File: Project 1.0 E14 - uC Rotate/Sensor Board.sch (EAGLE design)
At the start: 98 parts, among them IC1 LT1963EST-1.5, IC2 LT1963EST-1.5, IC4 LT1963EST-1.5

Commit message: Sensor Test Board: Selected humididty sensor and connected all relevent traces, added two humidity sensors to the libray (Si7005, Si7013). Changed hibernation module crystal to a 2-SMD package and rearanged relevent areas. Added 3 indicator LEDs to pins 57 - 59. Renamed and cleaned up schematic pages (now 7 pages labled by sensor type as apposed to manufacturer. Removed all 3.0V traces and supply and repplaced by 3.3V supply. Most 3.3V traces now routed but waiting for final power consuption calculations before completion. Changed power and programing connectors to smaller profile connectors (1 mm pitch) reducing required space, and cleaned up respective areas. Moved MAG3110 to top of board to for greater seperation from Si7013.
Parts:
- removed U$16: 5023520200, Kas-Connectors:5023520200
- removed U$20: 5023520410, Kas-Connectors:5023520410
- added J1: 501568-0207, Kas-Connectors:501568-0207
- added LED2, LED3, LED4: Green, eagle-ltspice:LED_ESML0603
- added R12, R13, R14: 10k, Kas-Passives:RESISTOR
- added U$7: 501568-0407, Kas-Connectors:501568-0407
- U$12: device Kas-Crystal:AB26TRB -> Kas-Crystal:ABS07L
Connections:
- removed net N$13: C41.2, C42.1, U$11.GNDX
- new net IND-LED-1: LED2.A, U$11.PE4
- new net IND-LED-2: LED3.A, U$11.PB4
- new net IND-LED-3: LED4.A, U$11.PB5
- new net N$29: LED4.C, R14.2
- new net N$31: LED3.C, R13.2
- new net N$35: LED2.C, R12.2
- net 3.0V: no longer R9.2, U$17.VDD_IO, U$2.VDDIO
- net 3.3V: now also U$17.VDD_IO, U$2.VDDIO
- net GND: now also C41.2, C42.1, J1.1, R12.1, R13.1, R14.1, R9.2, U$11.GNDX; no longer U$16.1
- net N$19: now also J1.2; no longer U$16.2
- net SWCLK: now also U$7.1; no longer U$20.1
- net SWDIO: now also U$7.2; no longer U$20.2
- net SWO: now also U$7.4; no longer U$20.4
- net TDI: now also U$7.3; no longer U$20.3
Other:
- moved on the sheet: LED1, R7

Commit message: Sensor Test Board: All parts have had their connections reviewed and tickets have been creted were necesery. Componnet footprints that needed checking have been checked and corrected as needed. Any misnamed pads have also been corrected. Missing net names were named and updated.
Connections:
- net CS-ADT7301 renamed !CS-ADT7301
- net CS-ADXL362 renamed !CS-ADXL362
- removed net 3.0V: IC1G$1.OUT
- removed net CS-H3LIS331DLTR: U$2.CS, U$21.1
- removed net CS-LIS3DH: U$21.6, U$9.CS
- removed net CS-LPS331: U$21.8, U$4.CS
- removed net CS-LS3GD20: U$21.7, U$3.CS
- removed net CS-LSM303: U$21.5, U$6.CS
- removed net CS-LSM9D30-G: U$17.CS_G, U$21.2
- removed net CS-LSM9DS0-XM: U$17.CS_XM, U$21.3
- removed net CS-MAX21000: U$19.CS, U$21.4
- removed net N$2: C52.1, U$15.VDD
- new net !CS-H3LIS331DLTR: U$2.!CS, U$21.1
- new net !CS-LIS3DH: U$21.6, U$9.!CS
- new net !CS-LPS331: U$21.8, U$4.!CS
- new net !CS-LS3GD20: U$21.7, U$3.!CS
- new net !CS-LSM303: U$21.5, U$6.!CS
- new net !CS-LSM9D30-G: U$17.!CS_G, U$21.2
- new net !CS-LSM9DS0-XM: U$17.!CS_XM, U$21.3
- new net !CS-MAX21000: U$19.!CS, U$21.4
- net 3.3V: now also C52.1, U$15.VDD, U$19.VDDIO, U$2.RSVD#1, U$22.VSNS
- net GND: now also U$10.RSVD$1, U$19.RSVD#0, U$2.RSVD#0, U$8.NC
- net SD-CS: now also U$18.!CS; no longer U$18.CS
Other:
- moved on the sheet: C52, U$21

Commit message: Sensor Test Board: Closed tickets 2, 17, 18, 21, 25 and 26. Changed sensor's designations to U from undifined.
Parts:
- renumbered U$1 to U1, U$10 to U10, U$11 to U11, U$14 to U14, U$15 to U15, U$17 to U17, U$18 to J3, U$19 to U19, U$2 to U2, U$21 to U21, U$22 to U22, U$3 to U3, U$4 to U4, U$5 to U5, U$6 to U6, U$7 to U7, U$8 to U8, U$9 to U9
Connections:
- removed net DEN-L3GD: U3.DEN
- net GND: now also U11.!WAKE, U11.PD4, U11.PD5, U3.DEN

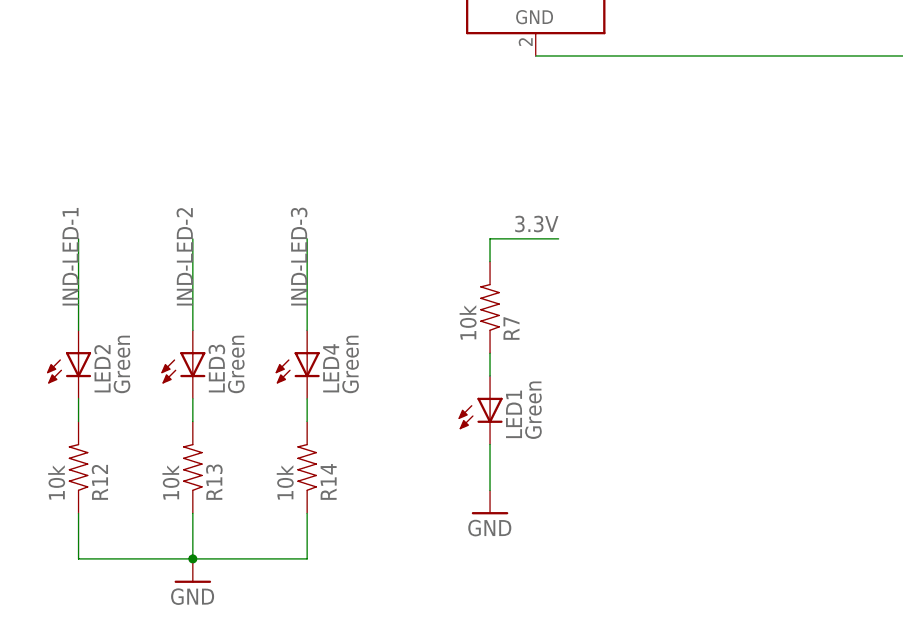
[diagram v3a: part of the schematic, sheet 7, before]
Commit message: Sensor Test Board: Resolved tickets 23, 20 and 19. The UART connection was moved to PIN 43 and 44 from 45,46 and a connector was added while the test points were moved lower to accomidate the connector.The indicator LEDs were moved from PB4, PB5 and PE4 to PB0 - PB3 with the addition one one more indication LED. The STLM20 was also moved to resolve ticket 19 and is now placed closer to PB4.
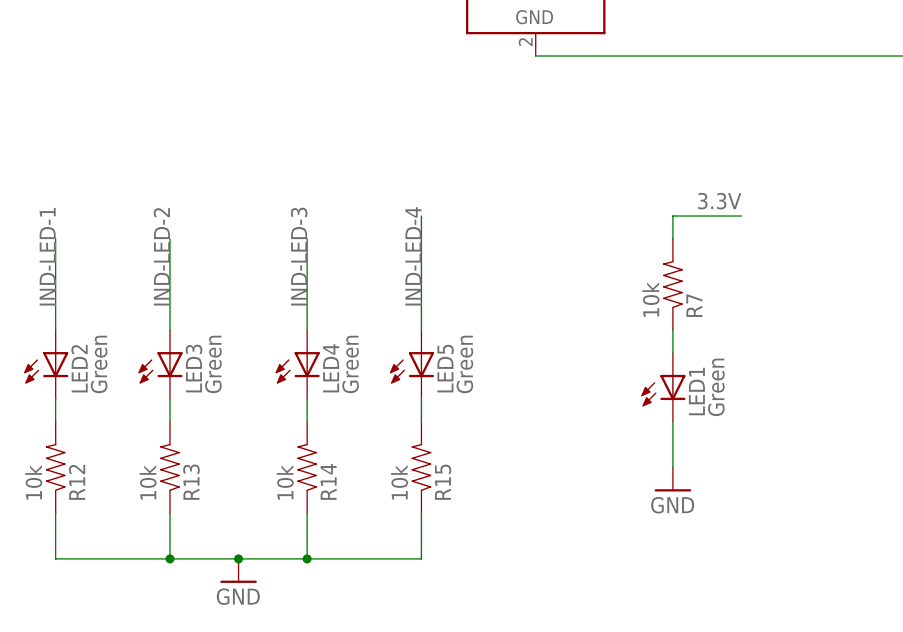
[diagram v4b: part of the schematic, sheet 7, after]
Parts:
- added J2: 501568-0207, Kas-Connectors:501568-0207
- added LED5: Green, eagle-ltspice:LED_ESML0603
- added R15: 10k, Kas-Passives:RESISTOR
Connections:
- removed net U1RX: TP8.P$1, U11.PB0
- removed net U1TX: TP7.P$1, U11.PB1
- new net IND-LED-4: LED5.A, U11.PB3
- new net N$18: LED5.C, R15.2
- new net U6RX: J2.1, TP8.P$1, U11.PD4
- new net U6TX: J2.2, TP7.P$1, U11.PD5
- net ANALOG-OUT-STLM20: now also U11.PB4; no longer U11.PB3
- net GND: now also R15.1, U17.INT_G; no longer R9.2, U11.PD4, U11.PD5
- net IND-LED-1: now also U11.PB0; no longer U11.PE4
- net IND-LED-2: now also U11.PB1; no longer U11.PB4
- net IND-LED-3: now also U11.PB2; no longer U11.PB5
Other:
- moved on the sheet: LED1, LED2, LED3, R11, R12, R13, R7, R9, TP7, TP8

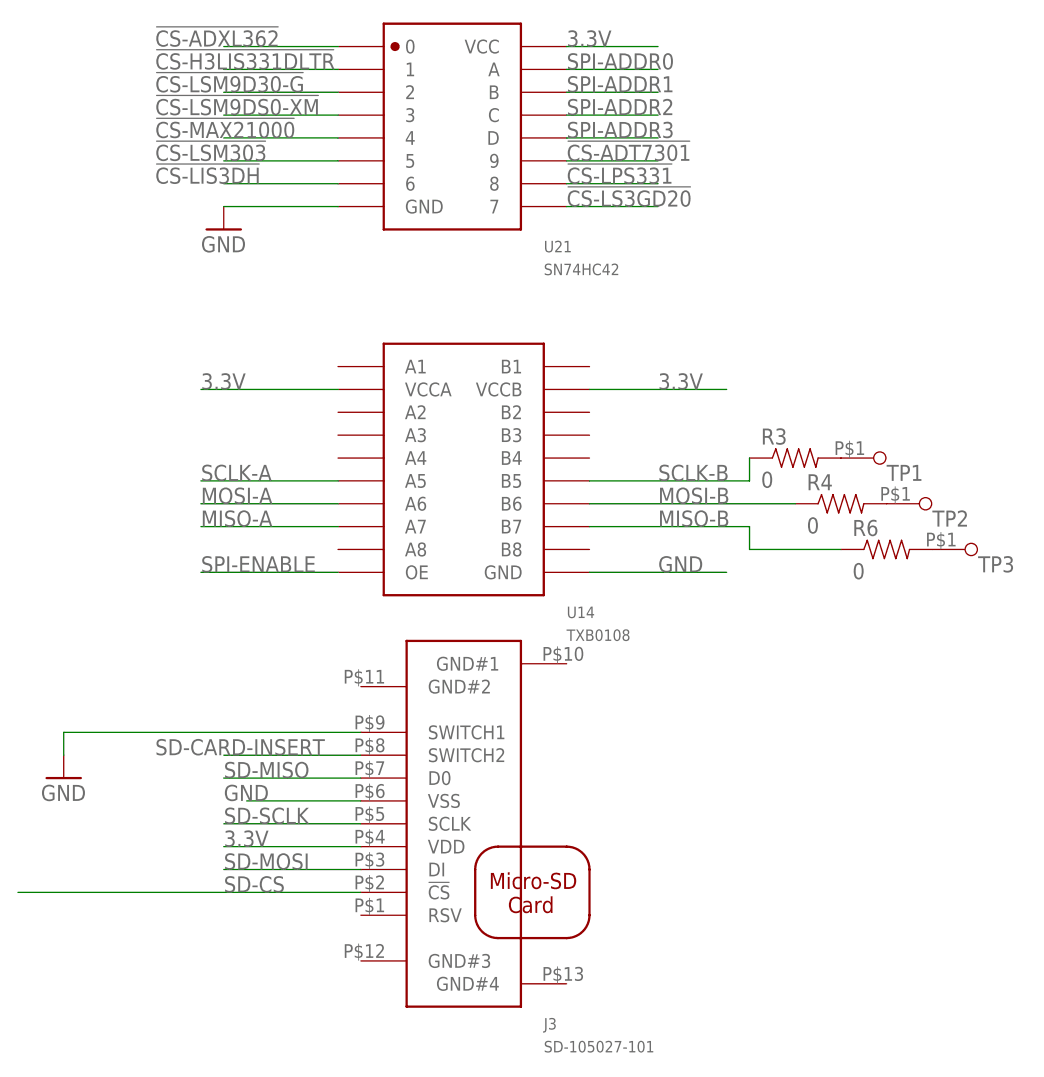
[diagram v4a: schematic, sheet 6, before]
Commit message: Sensor Test Board: Moved connections on TXB0108 to allow for simpler grounding of unused connections
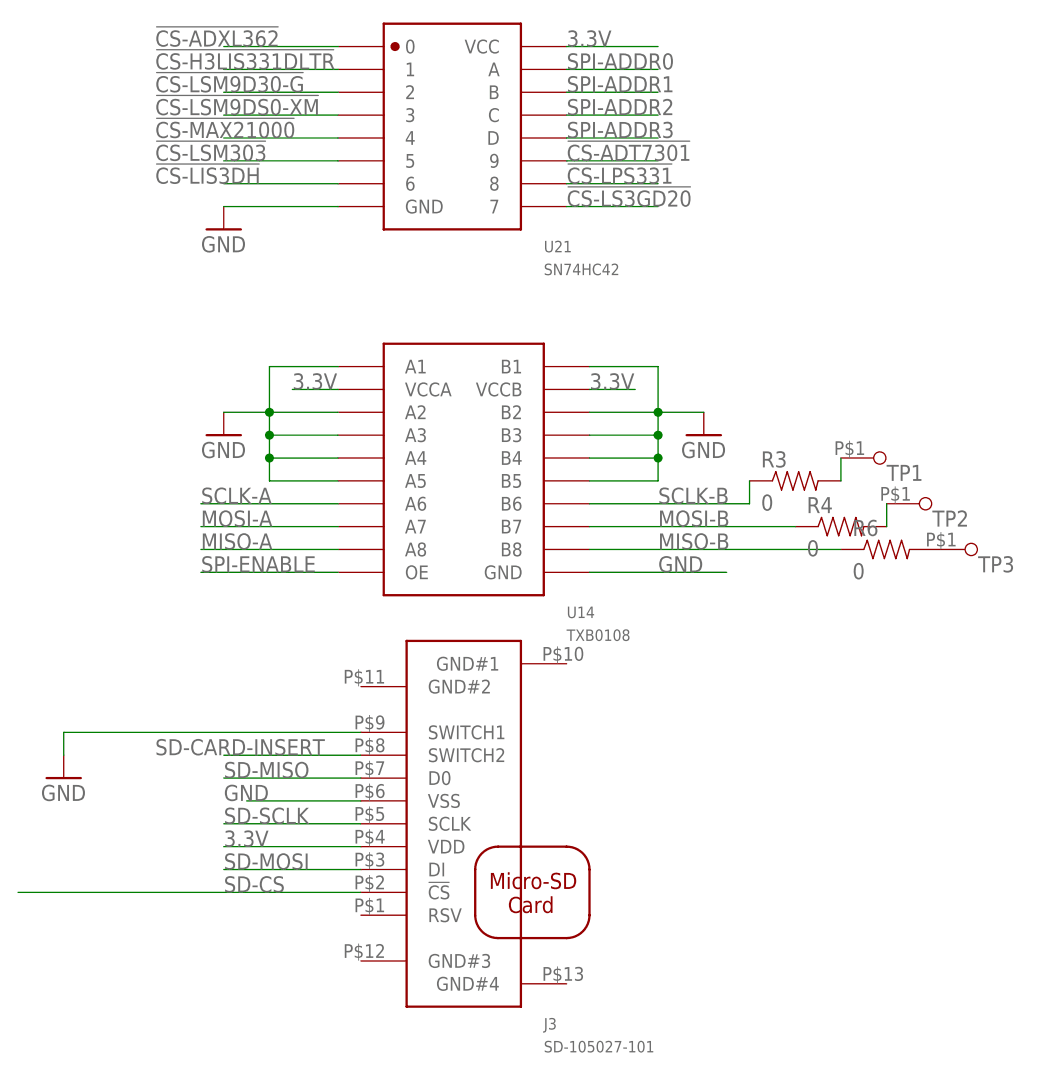
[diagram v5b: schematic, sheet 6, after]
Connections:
- net GND: now also U14.A1, U14.A2, U14.A3, U14.A4, U14.A5, U14.B1, U14.B2, U14.B3, U14.B4, U14.B5
- net MISO-A: now also U14.A8; no longer U14.A7
- net MISO-B: now also U14.B8; no longer U14.B7
- net MOSI-A: now also U14.A7; no longer U14.A6
- net MOSI-B: now also U14.B7; no longer U14.B6
- net SCLK-A: now also U14.A6; no longer U14.A5
- net SCLK-B: now also U14.B6; no longer U14.B5
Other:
- moved on the sheet: R3, R4
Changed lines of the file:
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@@
 <part name="LED5" library="eagle-ltspice" deviceset="LED_E" device="SML0603" value="Green"/>
 <part name="R15" library="Kas-Passives" deviceset="RESISTOR" device="" value="10k"/>
+<part name="GND50" library="SparkFun-Aesthetics" deviceset="GND" device=""/>
+<part name="GND51" library="SparkFun-Aesthetics" deviceset="GND" device=""/>
 </parts>
 <sheets>
@@
 <instance part="TP2" gate="G$1" x="53.34" y="-5.08"/>
 <instance part="TP3" gate="G$1" x="58.42" y="-10.16"/>
-<instance part="R3" gate="G$1" x="38.1" y="0"/>
-<instance part="R4" gate="G$1" x="43.18" y="-5.08"/>
+<instance part="R3" gate="G$1" x="38.1" y="-2.54"/>
+<instance part="R4" gate="G$1" x="43.18" y="-7.62"/>
 <instance part="R6" gate="G$1" x="48.26" y="-10.16"/>
 <instance part="U21" gate="G$1" x="0" y="35.56"/>
 <instance part="GND11" gate="1" x="-25.4" y="25.4"/>
+<instance part="GND50" gate="1" x="-25.4" y="2.54"/>
+<instance part="GND51" gate="1" x="27.94" y="2.54"/>
 </instances>
 <busses>
@@
 <pinref part="GND11" gate="1" pin="GND"/>
 </segment>
+<segment>
+<pinref part="U14" gate="G$1" pin="A2"/>
+<wire x1="-12.7" y1="5.08" x2="-20.32" y2="5.08" width="0.1524" layer="91"/>
+<pinref part="U14" gate="G$1" pin="A3"/>
+<wire x1="-20.32" y1="5.08" x2="-20.32" y2="2.54" width="0.1524" layer="91"/>
+<wire x1="-20.32" y1="2.54" x2="-12.7" y2="2.54" width="0.1524" layer="91"/>
+<pinref part="U14" gate="G$1" pin="A4"/>
+<wire x1="-12.7" y1="0" x2="-20.32" y2="0" width="0.1524" layer="91"/>
+<wire x1="-20.32" y1="0" x2="-20.32" y2="2.54" width="0.1524" layer="91"/>
+<junction x="-20.32" y="2.54"/>
+<pinref part="U14" gate="G$1" pin="A5"/>
+<wire x1="-12.7" y1="-2.54" x2="-20.32" y2="-2.54" width="0.1524" layer="91"/>
+<wire x1="-20.32" y1="-2.54" x2="-20.32" y2="0" width="0.1524" layer="91"/>
+<junction x="-20.32" y="0"/>
+<wire x1="-20.32" y1="5.08" x2="-20.32" y2="10.16" width="0.1524" layer="91"/>
+<junction x="-20.32" y="5.08"/>
+<pinref part="U14" gate="G$1" pin="A1"/>
+<wire x1="-20.32" y1="10.16" x2="-12.7" y2="10.16" width="0.1524" layer="91"/>
+<pinref part="GND50" gate="1" pin="GND"/>
+<wire x1="-20.32" y1="5.08" x2="-25.4" y2="5.08" width="0.1524" layer="91"/>
+</segment>
+<segment>
+<pinref part="U14" gate="G$1" pin="B2"/>
+<wire x1="15.24" y1="5.08" x2="22.86" y2="5.08" width="0.1524" layer="91"/>
+<wire x1="22.86" y1="5.08" x2="22.86" y2="2.54" width="0.1524" layer="91"/>
+<pinref part="U14" gate="G$1" pin="B3"/>
+<wire x1="22.86" y1="2.54" x2="15.24" y2="2.54" width="0.1524" layer="91"/>
+<pinref part="U14" gate="G$1" pin="B4"/>
+<wire x1="15.24" y1="0" x2="22.86" y2="0" width="0.1524" layer="91"/>
+<wire x1="22.86" y1="0" x2="22.86" y2="2.54" width="0.1524" layer="91"/>
+<junction x="22.86" y="2.54"/>
+<pinref part="U14" gate="G$1" pin="B5"/>
+<wire x1="15.24" y1="-2.54" x2="22.86" y2="-2.54" width="0.1524" layer="91"/>
+<wire x1="22.86" y1="-2.54" x2="22.86" y2="0" width="0.1524" layer="91"/>
+<junction x="22.86" y="0"/>
+<pinref part="U14" gate="G$1" pin="B1"/>
+<wire x1="15.24" y1="10.16" x2="22.86" y2="10.16" width="0.1524" layer="91"/>
+<wire x1="22.86" y1="10.16" x2="22.86" y2="5.08" width="0.1524" layer="91"/>
+<junction x="22.86" y="5.08"/>
+<pinref part="GND51" gate="1" pin="GND"/>
+<wire x1="27.94" y1="5.08" x2="22.86" y2="5.08" width="0.1524" layer="91"/>
+</segment>
 </net>
 <net name="MOSI-B" class="0">
 <segment>
-<label x="22.86" y="-5.08" size="1.778" layer="95"/>
-<pinref part="U14" gate="G$1" pin="B6"/>
-<wire x1="38.1" y1="-5.08" x2="15.24" y2="-5.08" width="0.1524" layer="91"/>
+<label x="22.86" y="-7.62" size="1.778" layer="95"/>
+<wire x1="38.1" y1="-7.62" x2="15.24" y2="-7.62" width="0.1524" layer="91"/>
 <pinref part="R4" gate="G$1" pin="1"/>
+<pinref part="U14" gate="G$1" pin="B7"/>
 </segment>
 </net>
 <net name="MISO-B" class="0">
 <segment>
-<label x="22.86" y="-7.62" size="1.778" layer="95"/>
-<wire x1="15.24" y1="-7.62" x2="33.02" y2="-7.62" width="0.1524" layer="91"/>
-<wire x1="33.02" y1="-7.62" x2="33.02" y2="-10.16" width="0.1524" layer="91"/>
-<wire x1="33.02" y1="-10.16" x2="43.18" y2="-10.16" width="0.1524" layer="91"/>
-<pinref part="U14" gate="G$1" pin="B7"/>
+<label x="22.86" y="-10.16" size="1.778" layer="95"/>
+<wire x1="15.24" y1="-10.16" x2="43.18" y2="-10.16" width="0.1524" layer="91"/>
 <pinref part="R6" gate="G$1" pin="1"/>
+<pinref part="U14" gate="G$1" pin="B8"/>
 </segment>
 </net>
@@
 <segment>
 <pinref part="U14" gate="G$1" pin="VCCA"/>
-<wire x1="-12.7" y1="7.62" x2="-27.94" y2="7.62" width="0.1524" layer="91"/>
-<label x="-27.94" y="7.62" size="1.778" layer="95"/>
+<wire x1="-12.7" y1="7.62" x2="-17.78" y2="7.62" width="0.1524" layer="91"/>
+<label x="-17.78" y="7.62" size="1.778" layer="95"/>
 </segment>
 <segment>
 <pinref part="U14" gate="G$1" pin="VCCB"/>
-<wire x1="15.24" y1="7.62" x2="30.48" y2="7.62" width="0.1524" layer="91"/>
-<label x="22.86" y="7.62" size="1.778" layer="95"/>
+<wire x1="15.24" y1="7.62" x2="20.32" y2="7.62" width="0.1524" layer="91"/>
+<label x="15.24" y="7.62" size="1.778" layer="95"/>
 </segment>
 <segment>
@@
 <net name="SCLK-B" class="0">
 <segment>
-<label x="22.86" y="-2.54" size="1.778" layer="95"/>
-<wire x1="15.24" y1="-2.54" x2="33.02" y2="-2.54" width="0.1524" layer="91"/>
-<wire x1="33.02" y1="-2.54" x2="33.02" y2="0" width="0.1524" layer="91"/>
-<pinref part="U14" gate="G$1" pin="B5"/>
+<label x="22.86" y="-5.08" size="1.778" layer="95"/>
+<wire x1="15.24" y1="-5.08" x2="33.02" y2="-5.08" width="0.1524" layer="91"/>
+<wire x1="33.02" y1="-5.08" x2="33.02" y2="-2.54" width="0.1524" layer="91"/>
 <pinref part="R3" gate="G$1" pin="1"/>
+<pinref part="U14" gate="G$1" pin="B6"/>
 </segment>
 </net>
@@
 <net name="MISO-A" class="0">
 <segment>
-<label x="-27.94" y="-7.62" size="1.778" layer="95"/>
-<wire x1="-12.7" y1="-7.62" x2="-27.94" y2="-7.62" width="0.1524" layer="91"/>
-<pinref part="U14" gate="G$1" pin="A7"/>
+<label x="-27.94" y="-10.16" size="1.778" layer="95"/>
+<pinref part="U14" gate="G$1" pin="A8"/>
+<wire x1="-12.7" y1="-10.16" x2="-27.94" y2="-10.16" width="0.1524" layer="91"/>
 </segment>
 </net>
@@
 <net name="SCLK-A" class="0">
 <segment>
-<label x="-27.94" y="-2.54" size="1.778" layer="95"/>
-<wire x1="-12.7" y1="-2.54" x2="-27.94" y2="-2.54" width="0.1524" layer="91"/>
-<pinref part="U14" gate="G$1" pin="A5"/>
-</segment>
-</net>
-<net name="MOSI-A" class="0">
-<segment>
 <label x="-27.94" y="-5.08" size="1.778" layer="95"/>
 <pinref part="U14" gate="G$1" pin="A6"/>
-<wire x1="-27.94" y1="-5.08" x2="-12.7" y2="-5.08" width="0.1524" layer="91"/>
+<wire x1="-12.7" y1="-5.08" x2="-27.94" y2="-5.08" width="0.1524" layer="91"/>
+</segment>
+</net>
+<net name="MOSI-A" class="0">
+<segment>
+<label x="-27.94" y="-7.62" size="1.778" layer="95"/>
+<wire x1="-27.94" y1="-7.62" x2="-12.7" y2="-7.62" width="0.1524" layer="91"/>
+<pinref part="U14" gate="G$1" pin="A7"/>
 </segment>
 </net>
@@
 <pinref part="R3" gate="G$1" pin="2"/>
 <pinref part="TP1" gate="G$1" pin="P$1"/>
+<wire x1="43.18" y1="-2.54" x2="43.18" y2="0" width="0.1524" layer="91"/>
 </segment>
 </net>
@@
 <pinref part="R4" gate="G$1" pin="2"/>
 <pinref part="TP2" gate="G$1" pin="P$1"/>
-</segment>
-</net>
+<wire x1="48.26" y1="-7.62" x2="48.26" y2="-5.08" width="0.1524" layer="91"/>
+</segment>
+</net>
